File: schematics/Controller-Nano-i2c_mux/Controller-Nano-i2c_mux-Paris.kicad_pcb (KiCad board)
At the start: 2 copper layers, 37.8 x 60.5 mm, 20 parts, among them P1 CONN_02X04, P2 CONN_02X04, U1 Arduino_Nano, U2 PCA9544A

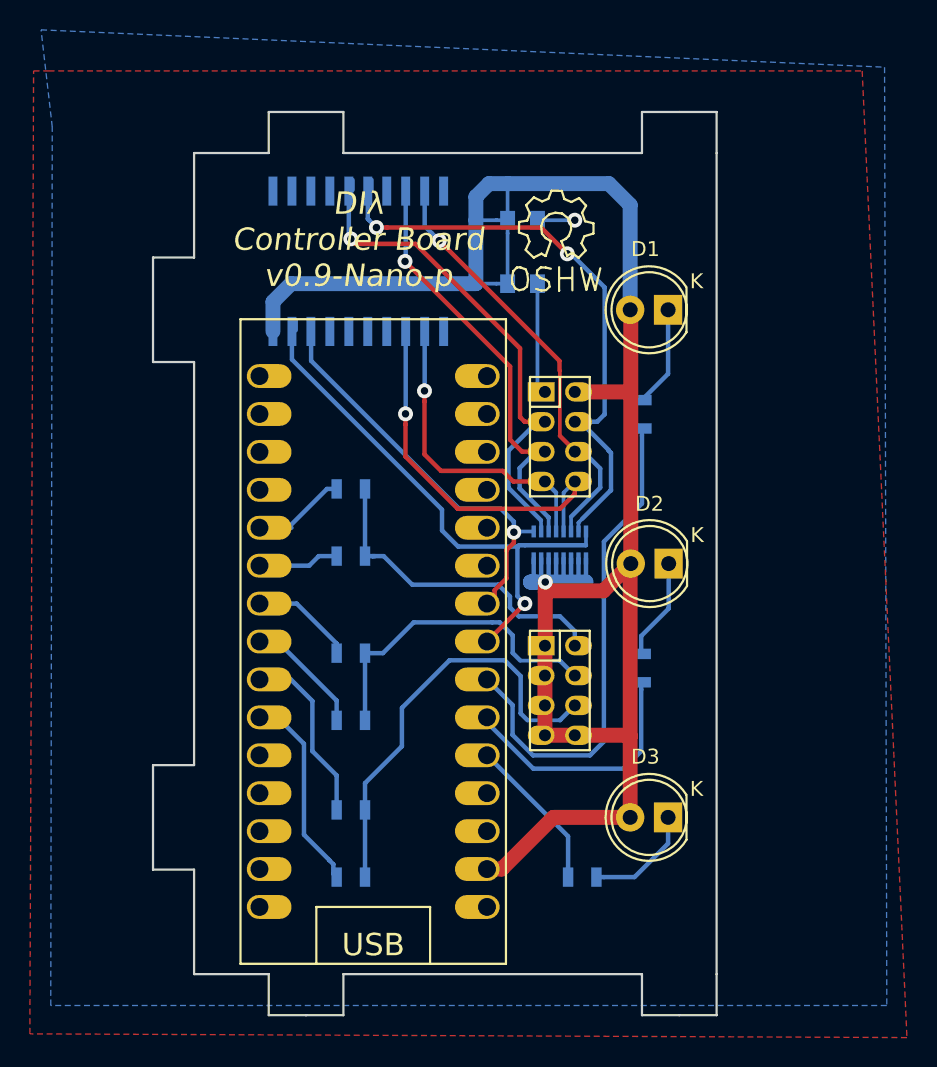
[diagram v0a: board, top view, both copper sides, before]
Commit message: schematics: update LED connections, use 4x resistor arrays
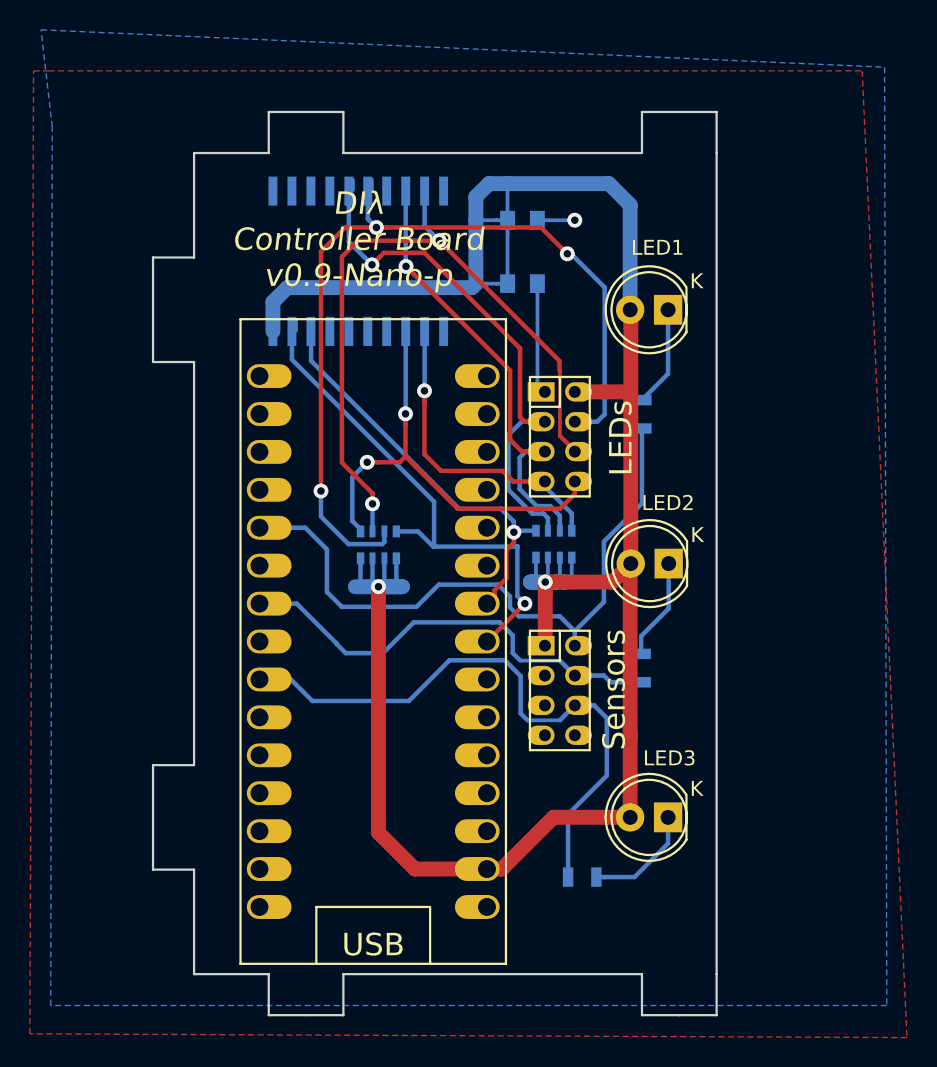
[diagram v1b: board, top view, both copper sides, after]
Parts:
- removed R1, R3, R5: 330, Resistors_SMD:R_0805
- removed R2, R4, R6: 470, Resistors_SMD:R_0805
- removed REF**: Symbol_OSHW-Logo_SilkScreen, Symbols:Symbol_OSHW-Logo_SilkScreen
- added RP2: R_PACK4, Resistors_SMD:R_Array_Convex_4x0603, B.Cu at (152.3, 89.2)
- R7, R8, R9: value R -> 220
- RP1: value R_PACK8 -> R_PACK4; footprint Resistors_SMD:R_Array_Convex_8x0602 -> Resistors_SMD:R_Array_Convex_4x0603
- moved RP1 0.40 mm to (164.1, 89.2)
- renumbered D1 to LED1, D2 to LED2, D3 to LED3
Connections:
- P2 pad 2: Net-(P2-Pad2) -> LED1
- P2 pad 3: +3V3 -> (no net)
- P2 pad 4: Net-(P2-Pad4) -> LED2
- P2 pad 5: +3V3 -> (no net)
- P2 pad 6: Net-(P2-Pad6) -> LED3
- P2 pad 7: +3V3 -> (no net)
- P2 pad 8: +3V3 -> (no net)
- R7 pad 2: Net-(R7-Pad2) -> LED1
- R8 pad 2: Net-(R8-Pad2) -> LED2
- R9 pad 2: Net-(R9-Pad2) -> LED3
- RP1 pad 5: SC2 -> +3V3
- RP1 pad 6: SC1 -> +3V3
- RP1 pad 7: SC0 -> +3V3
- RP1 pad 8: SDA -> +3V3
- U1 pad 1: Net-(U1-Pad1) -> (no net)
- U1 pad 10: Net-(R6-Pad1) -> (no net)
- U1 pad 18: Net-(U1-Pad18) -> (no net)
- U1 pad 19: Net-(U1-Pad19) -> (no net)
- U1 pad 2: Net-(U1-Pad2) -> (no net)
- U1 pad 20: Net-(R9-Pad2) -> (no net)
- U1 pad 21: Net-(R8-Pad2) -> (no net)
- U1 pad 22: Net-(R7-Pad2) -> (no net)
- U1 pad 25: Net-(U1-Pad25) -> (no net)
- U1 pad 26: Net-(U1-Pad26) -> (no net)
- U1 pad 27: Net-(U1-Pad27) -> (no net)
- U1 pad 28: Net-(U1-Pad28) -> (no net)
- U1 pad 29: Net-(U1-Pad29) -> (no net)
- U1 pad 3: Net-(U1-Pad3) -> (no net)
- U1 pad 30: Net-(U1-Pad30) -> (no net)
- U1 pad 5: Net-(R1-Pad1) -> LED1
- U1 pad 6: Net-(R2-Pad1) -> (no net)
- U1 pad 7: Net-(R3-Pad1) -> LED2
- U1 pad 8: Net-(R4-Pad1) -> (no net)
- U1 pad 9: Net-(R5-Pad1) -> LED3
- U2 pad 11: Net-(U2-Pad11) -> (no net)
- U2 pad 14: Net-(U2-Pad14) -> (no net)
- U2 pad 15: Net-(U2-Pad15) -> (no net)
- U2 pad 16: Net-(U2-Pad16) -> (no net)
- U2 pad 17: Net-(U2-Pad17) -> (no net)
- U2 pad 4: Net-(U2-Pad4) -> (no net)
- U2 pad 7: Net-(U2-Pad7) -> (no net)
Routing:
- net LED1: track 0.00 -> 47.8 mm
- net LED3: track 0.00 -> 40.6 mm
- net Net-(R7-Pad2): track 33.5 -> 0.00 mm
- net LED2: track 0.00 -> 30.2 mm
- net Net-(P2-Pad6): track 28.8 -> 0.00 mm
- net Net-(P2-Pad2): track 22.2 -> 0.00 mm
- net Net-(P2-Pad4): track 21.6 -> 0.00 mm
- net SC1: track 28.8 -> 48.4 mm, vias 1 -> 2
- net +3V3: track 140.0 -> 159.4 mm, vias 1 -> 2
- net SC0: track 40.5 -> 59.3 mm, vias 2 -> 3
- net Net-(R8-Pad2): track 17.1 -> 0.00 mm
- net Net-(R6-Pad1): track 13.5 -> 0.00 mm
- net Net-(R5-Pad1): track 12.1 -> 0.00 mm
- net Net-(R9-Pad2): track 10.4 -> 0.00 mm
- net Net-(R1-Pad1): track 8.39 -> 0.00 mm
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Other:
- net class Power: trace_width 0.25 -> 1
- board text added: "LEDs"
- board text added: "Sensors"

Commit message: Schematics update
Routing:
- net LED2: track 30.2 -> 28.4 mm
- net LED3: track 40.6 -> 39.4 mm
- net +3V3: track 159.4 -> 158.2 mm
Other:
- board text added: "1"
